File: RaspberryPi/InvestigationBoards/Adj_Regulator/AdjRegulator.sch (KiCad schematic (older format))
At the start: 22 parts, among them P1 CONN_2, P2 CONN_13X2, P4 CONN_2, U1 LM22677, U3 MAX5437, U6 INA_220, U8 DS18B20

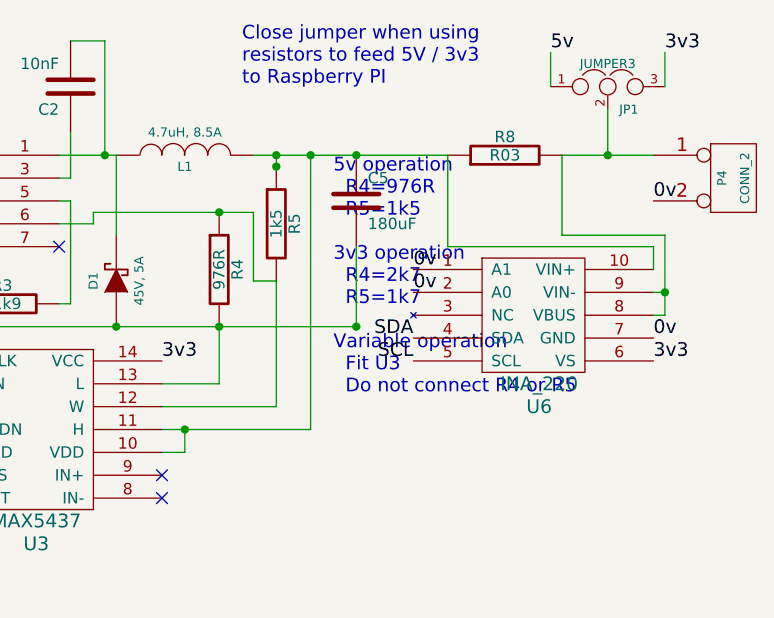
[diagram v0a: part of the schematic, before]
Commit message: Moved MAX-5437 VDD line to power and removed the 5v/3v3 selector for powering the PI.
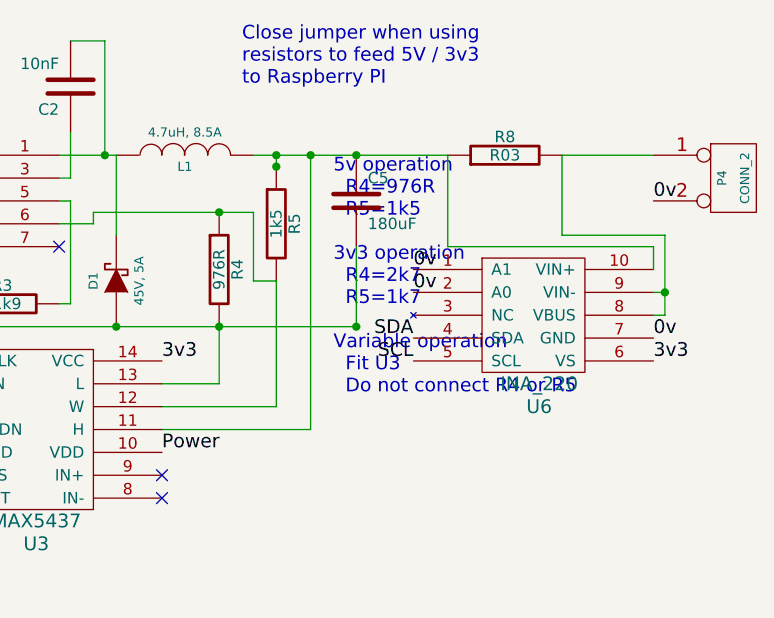
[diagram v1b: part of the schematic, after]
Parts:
- removed JP1: JUMPER3, symbol JUMPER3
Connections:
- net Power: now also U3.10 (VDD)
- net at C5.1, L1.2, R5.1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: no longer U3.10 (VDD)
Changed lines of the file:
@@
-EESchema Schematic File Version 2  date Fri 19 Apr 2013 08:55:30 BST
+EESchema Schematic File Version 2  date Sat 28 Sep 2013 22:20:46 BST
 LIBS:power
 LIBS:device
@@
 Sheet 1 1
 Title ""
-Date "19 apr 2013"
+Date "28 sep 2013"
 Rev ""
 Comp ""
@@
 Comment4 ""
 $EndDescr
-Connection ~ 10050 3150
+Text Label 8100 4450 0    60   ~ 0
+Power
 Wire Wire Line
 	3950 4600 4050 4600
@@
 Wire Wire Line
 	3550 4800 3400 4800
-Wire Wire Line
-	9800 2700 9800 2850
 Connection ~ 1300 3800
 Wire Wire Line
@@
 Wire Wire Line
 	6400 4550 6950 4550
-Connection ~ 8200 4350
-Wire Wire Line
-	8200 4350 8200 4450
-Wire Wire Line
-	8200 4450 8100 4450
 Wire Wire Line
 	6500 4150 6950 4150
@@
 Wire Wire Line
 	1300 3700 1300 3800
-Wire Wire Line
-	10050 2950 10050 3150
-Wire Wire Line
-	10300 2700 10300 2850
 Wire Wire Line
 	3850 4350 3550 4350
@@
 	0    -1   -1   0
 $EndComp
-$Comp
-L JUMPER3 JP1
-U 1 1 50E89148
-P 10050 2850
-F 0 "JP1" H 10100 2750 40  0000 L CNN
-F 1 "JUMPER3" H 10050 2950 40  0000 C CNN
-	1    10050 2850
-	1    0    0    -1
-$EndComp
-Text Label 10300 2700 0    60   ~ 0
-3v3
 Text Label 2600 4800 0    60   ~ 0
 0v
@@
 Text Label 3400 3800 0    60   ~ 0
 0v
-Text Label 9800 2700 0    60   ~ 0
-5v
 NoConn ~ 2600 4400
 $Comp
